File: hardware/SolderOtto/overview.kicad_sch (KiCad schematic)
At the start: 11 parts, among them X901 JBC-AM-SB, X902 JBC-AD-SF, X904 Binder_IP40_06, X905 Binder_IP40_07, X906 Binder_IP40_07, X907 Hirose RPC1-12RB-6P

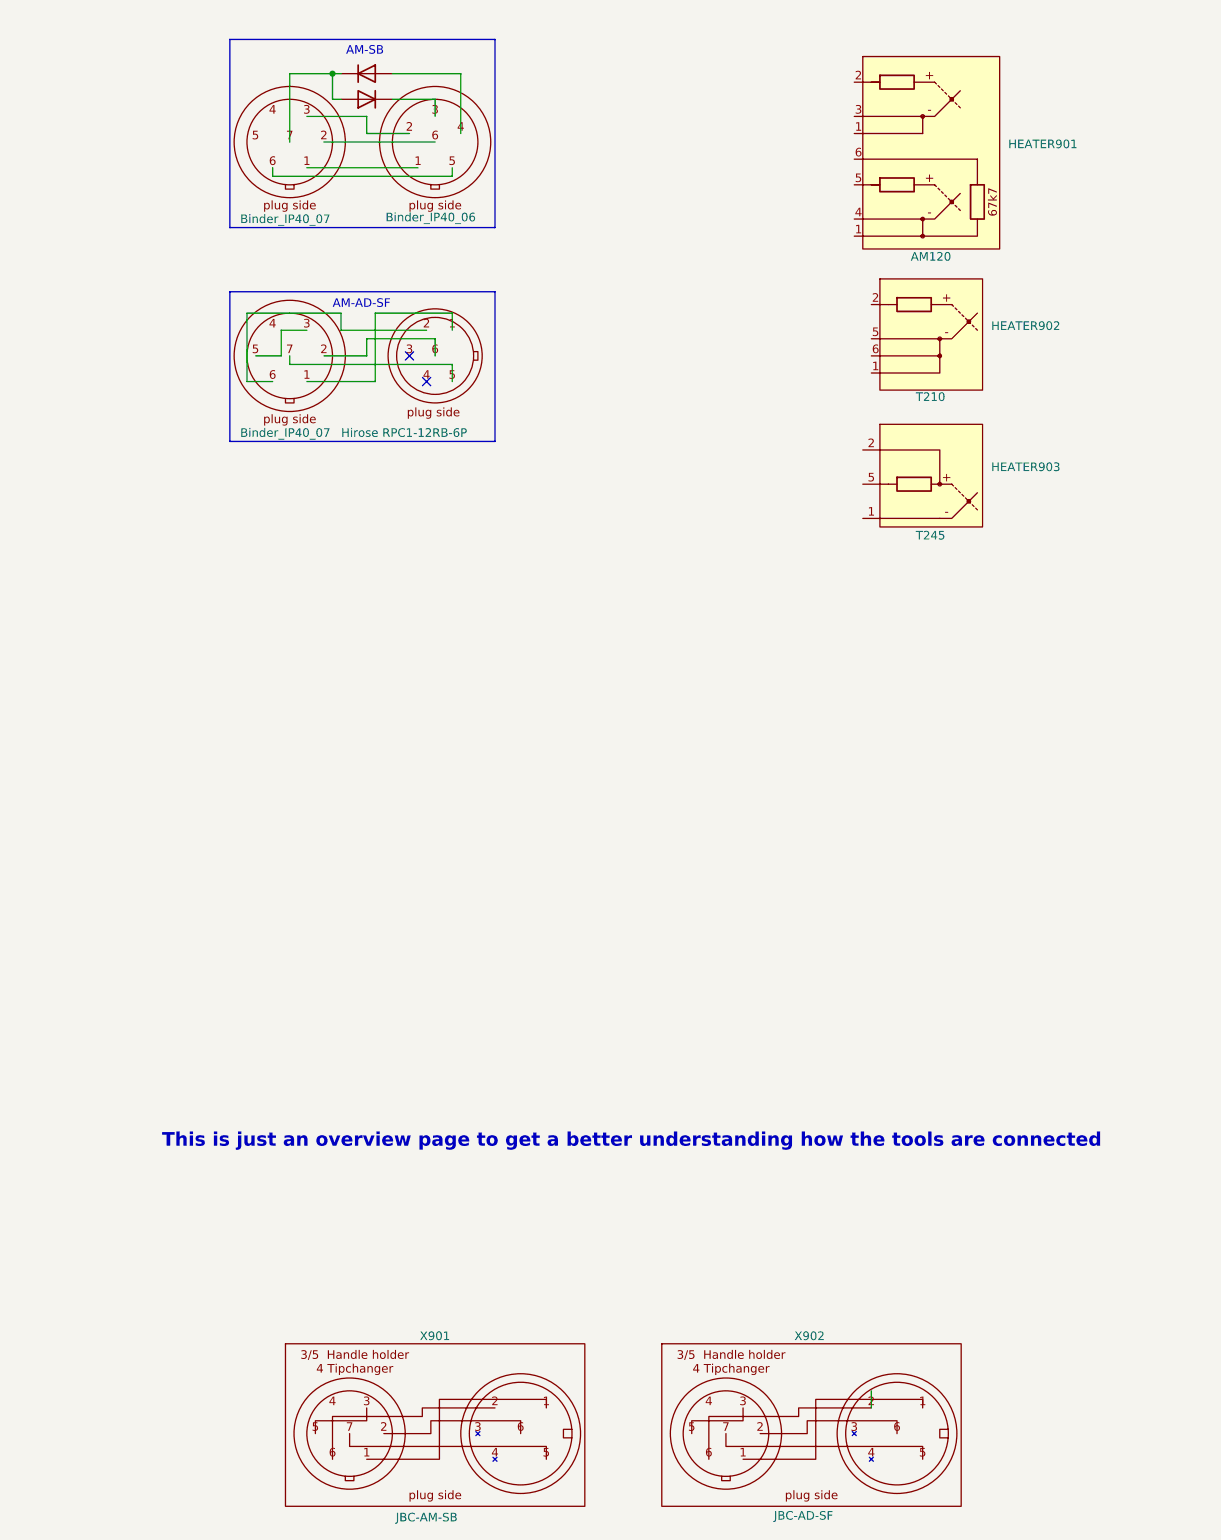
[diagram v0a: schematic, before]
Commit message: add support for tweezers AM-120
change mcu to stm32h573VI
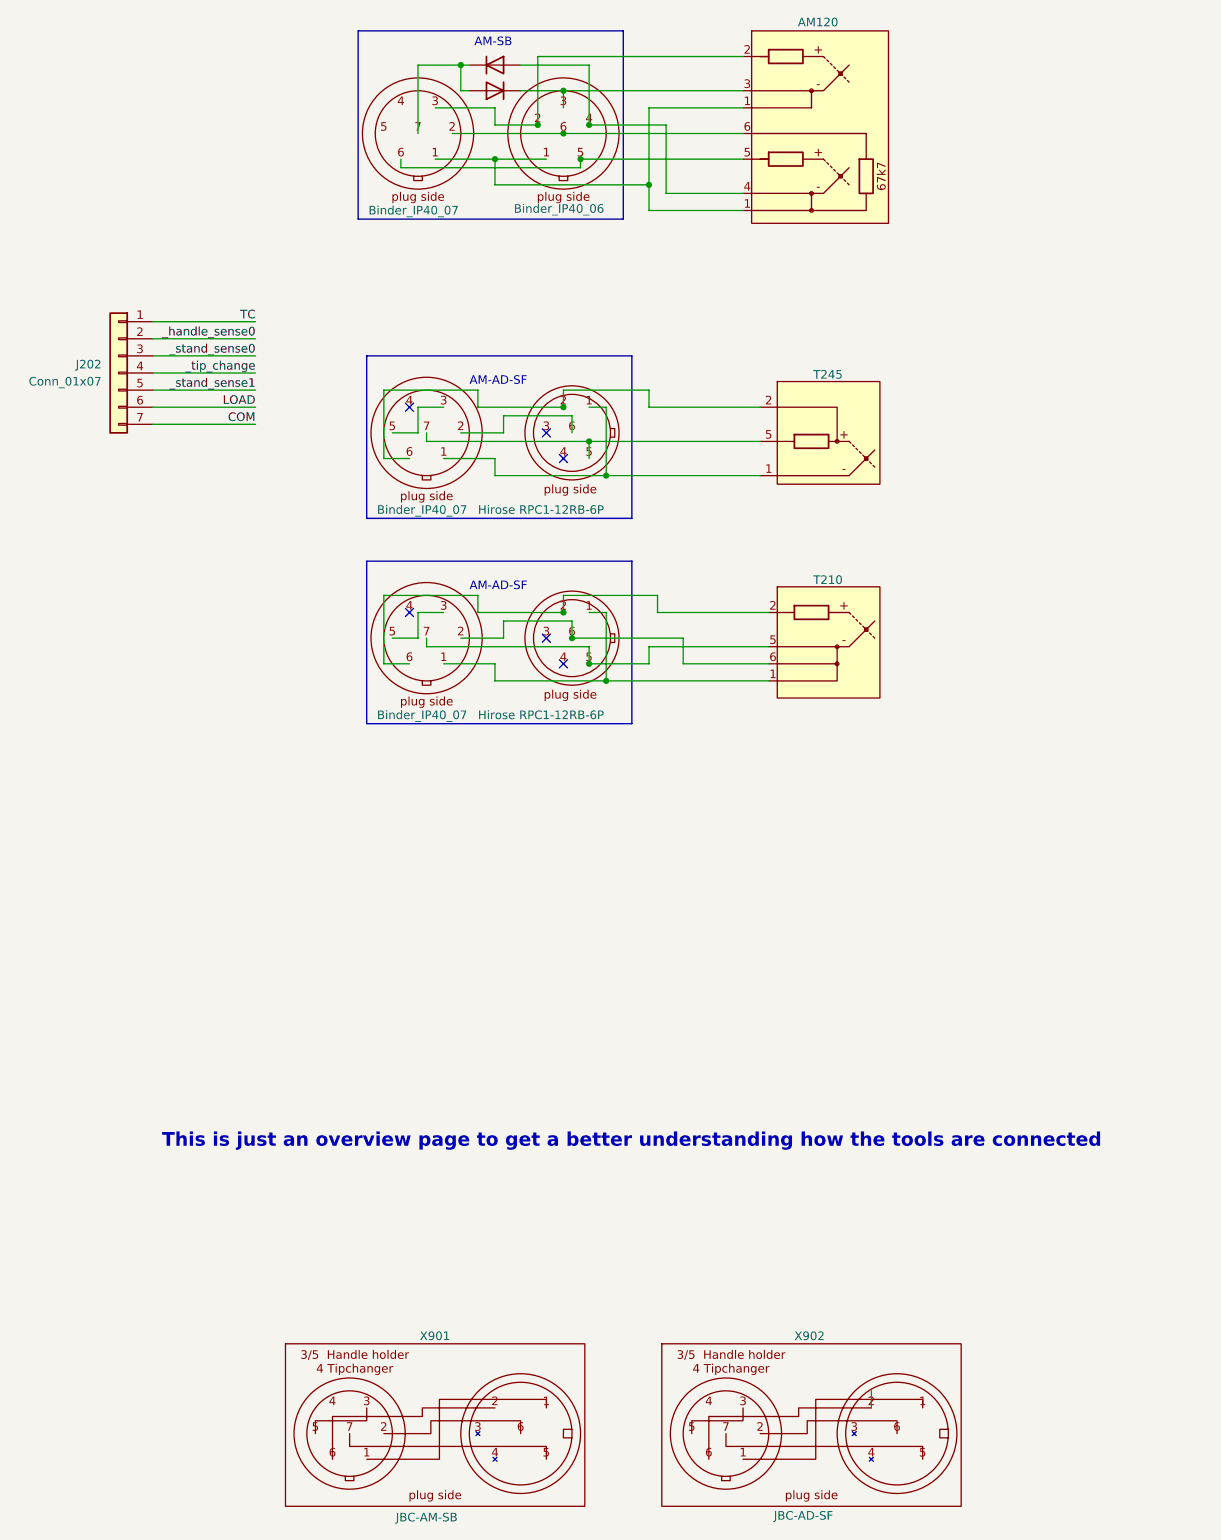
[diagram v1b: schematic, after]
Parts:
- added J202: Conn_01x07, Connector_Molex:Molex_Micro-Fit_3.0_43650-0715_1x07_P3.00mm_Vertical, symbol Connector_Generic:Conn_01x07
- added X201: Binder_IP40_07, symbol mylib_connectors:Binder_IP40_07
- added X202: Hirose RPC1-12RB-6P, symbol mylib_connectors:Hirose RPC1-12RB-6P
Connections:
- net at X906.1, X907.1: now also HEATER903.1
- net at X906.6, X907.2: now also HEATER903.2
- net at X906.7, X907.5: now also HEATER903.5
- net at D902.2 (A), X904.4: now also HEATER901.4
- net at X904.1, X905.1: now also HEATER901.1
- net at X904.2, X905.3: now also HEATER901.2
- net at D901.1 (K), X904.3: now also HEATER901.3
- net at X904.5, X905.6: now also HEATER901.5
- net at X904.6, X905.2: now also HEATER901.6
- net at HEATER902.1: now also X201.1, X202.1
- net at HEATER902.2: now also X201.6, X202.2
- net at HEATER902.5: now also X201.7, X202.5
- net at HEATER902.6: now also X201.2, X202.6
- new net: X201.3, X201.5
- new net COM: J202.7 (Pin_7)
- new net LOAD: J202.6 (Pin_6)
- new net TC: J202.1 (Pin_1)
- new net _handle_sense0: J202.2 (Pin_2)
- new net _stand_sense0: J202.3 (Pin_3)
- new net _stand_sense1: J202.5 (Pin_5)
- new net _tip_change: J202.4 (Pin_4)
- no-connect marks 2 -> 6

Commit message: save wip
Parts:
- added J203, J204: Conn_01x07, Connector_Molex:Molex_Micro-Fit_3.0_43650-0715_1x07_P3.00mm_Vertical, symbol Connector_Generic:Conn_01x07
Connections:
- net COM: now also J203.7 (Pin_7); no longer J202.7 (Pin_7)
- net LOAD: now also J203.6 (Pin_6); no longer J202.6 (Pin_6)
- net TC: now also J203.1 (Pin_1); no longer J202.1 (Pin_1)
- net _handle_sense0: now also J203.2 (Pin_2); no longer J202.2 (Pin_2)
- net _stand_sense0: now also J203.3 (Pin_3); no longer J202.3 (Pin_3)
- net _stand_sense1: now also J203.5 (Pin_5); no longer J202.5 (Pin_5)
- net _tip_change: now also J203.4 (Pin_4); no longer J202.4 (Pin_4)
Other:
- moved on the sheet: J202

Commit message: wip
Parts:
- removed D901, D902: D, symbol Device:D
- removed HEATER901: AM120, symbol mylib_connectors:JBC-AM120
- removed HEATER902: T210, symbol mylib_connectors:JBC-T210
- removed HEATER903: T245, symbol mylib_connectors:JBC-T245
- removed X201, X905, X906: Binder_IP40_07, symbol mylib_connectors:Binder_IP40_07
- removed X202, X907: Hirose RPC1-12RB-6P, symbol mylib_connectors:Hirose RPC1-12RB-6P
- removed X901: JBC-AM-SB, symbol mylib_connectors:JBC-AM-SB
- removed X902: JBC-AD-SF, symbol mylib_connectors:JBC-AD-SF
- removed X904: Binder_IP40_06, symbol mylib_connectors:Binder_IP40_06
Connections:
- no-connect marks 6 -> 0
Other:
- note removed: "AM-AD-SF"
- note removed: "AM-SB"
